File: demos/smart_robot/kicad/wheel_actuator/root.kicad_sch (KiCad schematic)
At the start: 9 parts, among them M1 WHEEL_MOTOR_DESIGN_ENVELOPE, U1 AT32M416, U2 DRV8323, U3 TCAN3413DR

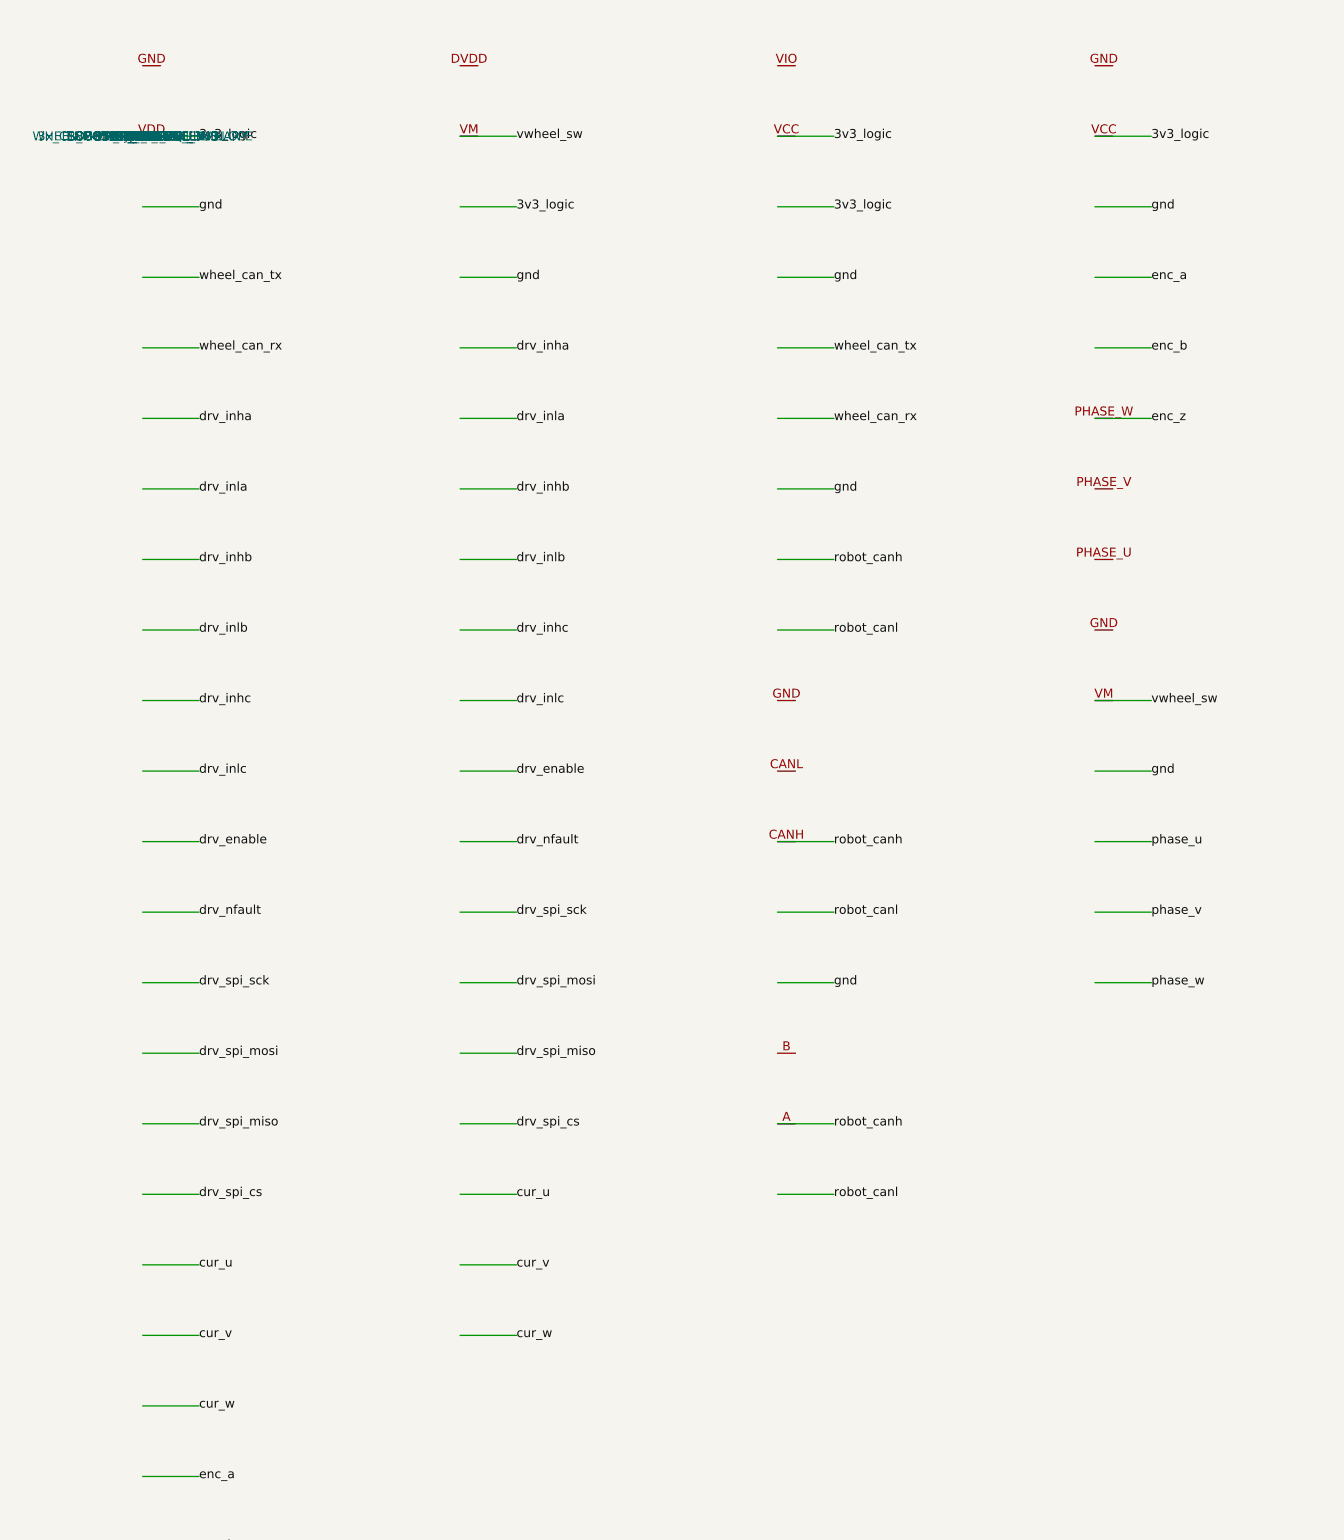
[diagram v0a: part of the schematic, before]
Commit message: Validate wheel current sense placement
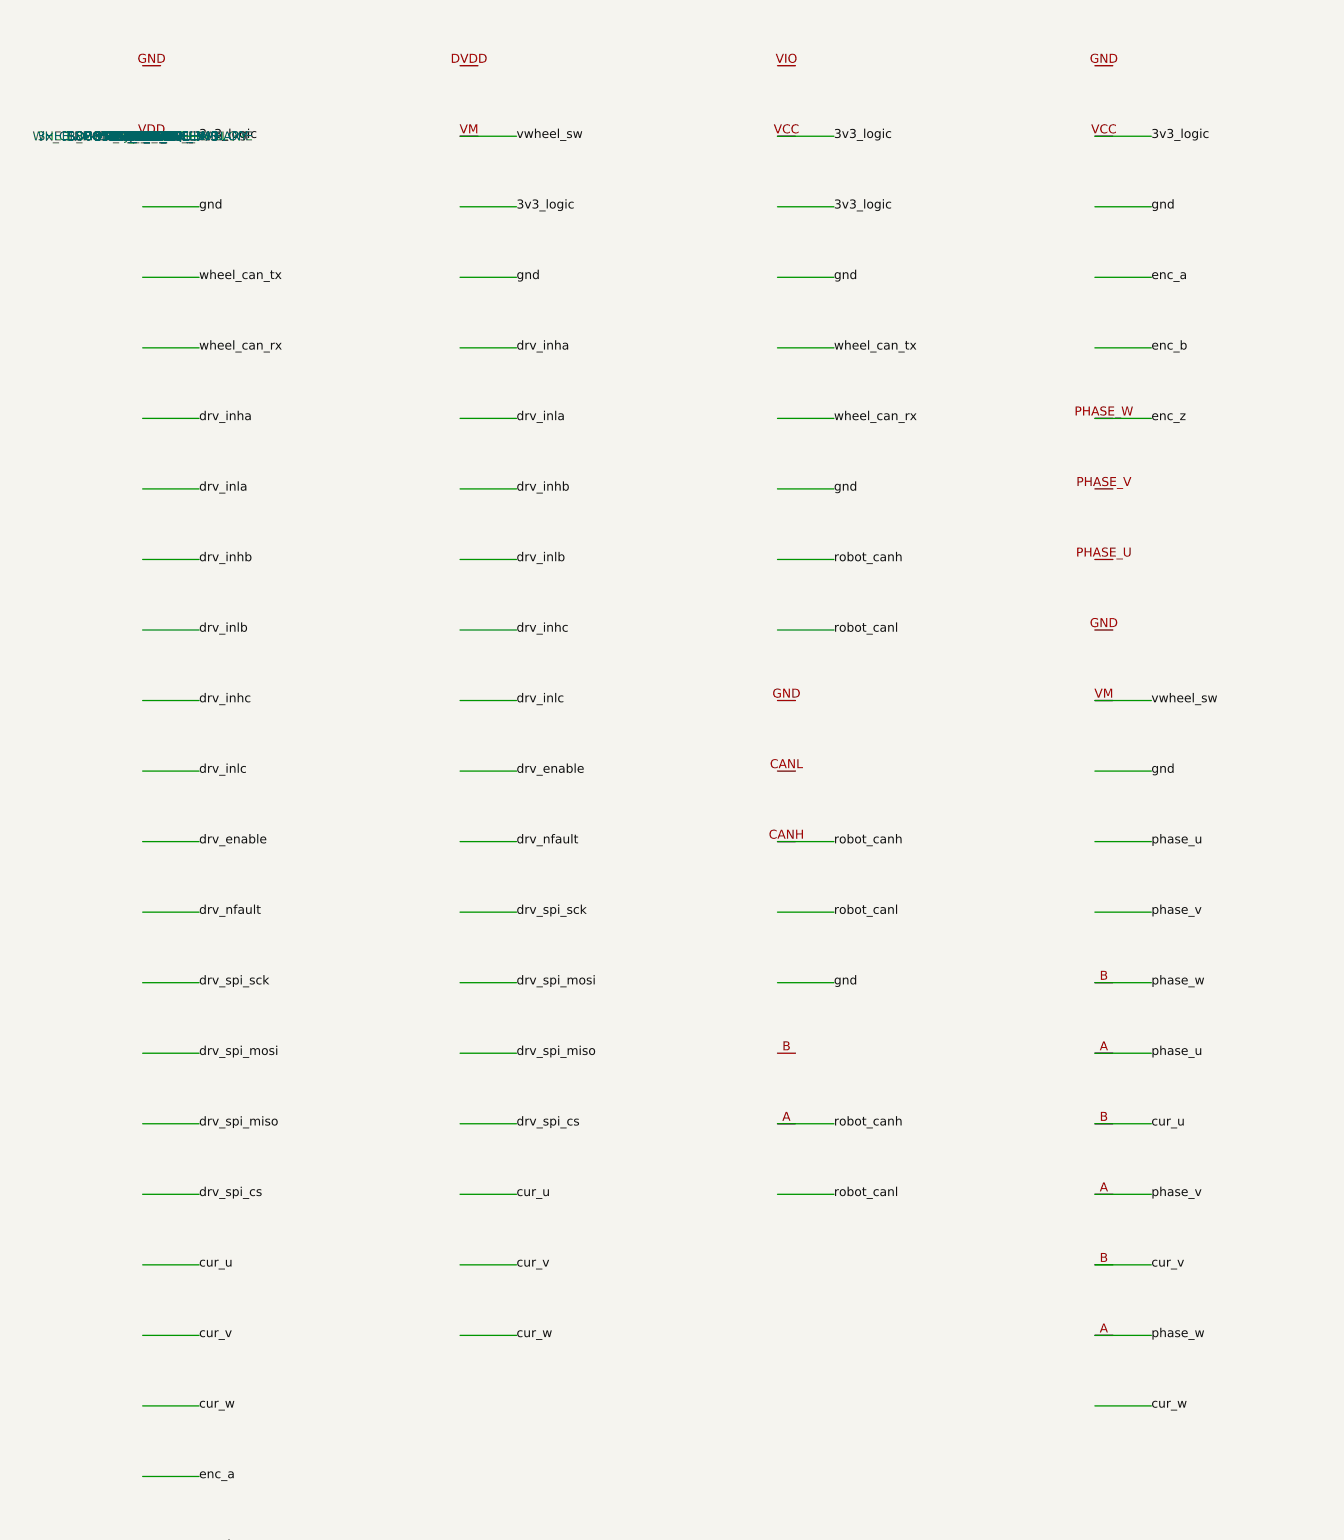
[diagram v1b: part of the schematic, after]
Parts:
- added RSHUNT_U, RSHUNT_V, RSHUNT_W: 5mR_1W, symbol CircuitCI:Resistor
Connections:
- net cur_u: now also RSHUNT_V.B
- net cur_v: now also RSHUNT_W.B
- net phase_u: now also RSHUNT_U.A
- net phase_v: now also RSHUNT_V.A
- net phase_w: now also RSHUNT_U.B, RSHUNT_W.A
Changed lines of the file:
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@@
     (property "Value" "3x_CSD88599Q5DC_PRELIMINARY")
     (pin "VM") (pin "GND") (pin "PHASE_U") (pin "PHASE_V") (pin "PHASE_W"))
+  (symbol (lib_id "CircuitCI:Resistor") (at 135 130 0)
+    (property "Reference" "RSHUNT_U")
+    (property "Value" "5mR_1W")
+    (pin "A") (pin "B"))
+  (symbol (lib_id "CircuitCI:Resistor") (at 135 150 0)
+    (property "Reference" "RSHUNT_V")
+    (property "Value" "5mR_1W")
+    (pin "A") (pin "B"))
+  (symbol (lib_id "CircuitCI:Resistor") (at 135 170 0)
+    (property "Reference" "RSHUNT_W")
+    (property "Value" "5mR_1W")
+    (pin "A") (pin "B"))
   (symbol (lib_id "CircuitCI:Wheel_Motor_Envelope") (at 180 80 0)
     (property "Reference" "M1")
@@
   (wire (pts (xy 135 110) (xy 143 110))) (label "phase_v" (at 143 110 0))
   (wire (pts (xy 135 120) (xy 143 120))) (label "phase_w" (at 143 120 0))
+  (wire (pts (xy 135 130) (xy 143 130))) (label "phase_u" (at 143 130 0))
+  (wire (pts (xy 135 140) (xy 143 140))) (label "cur_u" (at 143 140 0))
+  (wire (pts (xy 135 150) (xy 143 150))) (label "phase_v" (at 143 150 0))
+  (wire (pts (xy 135 160) (xy 143 160))) (label "cur_v" (at 143 160 0))
+  (wire (pts (xy 135 170) (xy 143 170))) (label "phase_w" (at 143 170 0))
+  (wire (pts (xy 135 180) (xy 143 180))) (label "cur_w" (at 143 180 0))
   (wire (pts (xy 180 0) (xy 188 0))) (label "vwheel_sw" (at 188 0 0))
   (wire (pts (xy 180 10) (xy 188 10))) (label "gnd" (at 188 10 0))

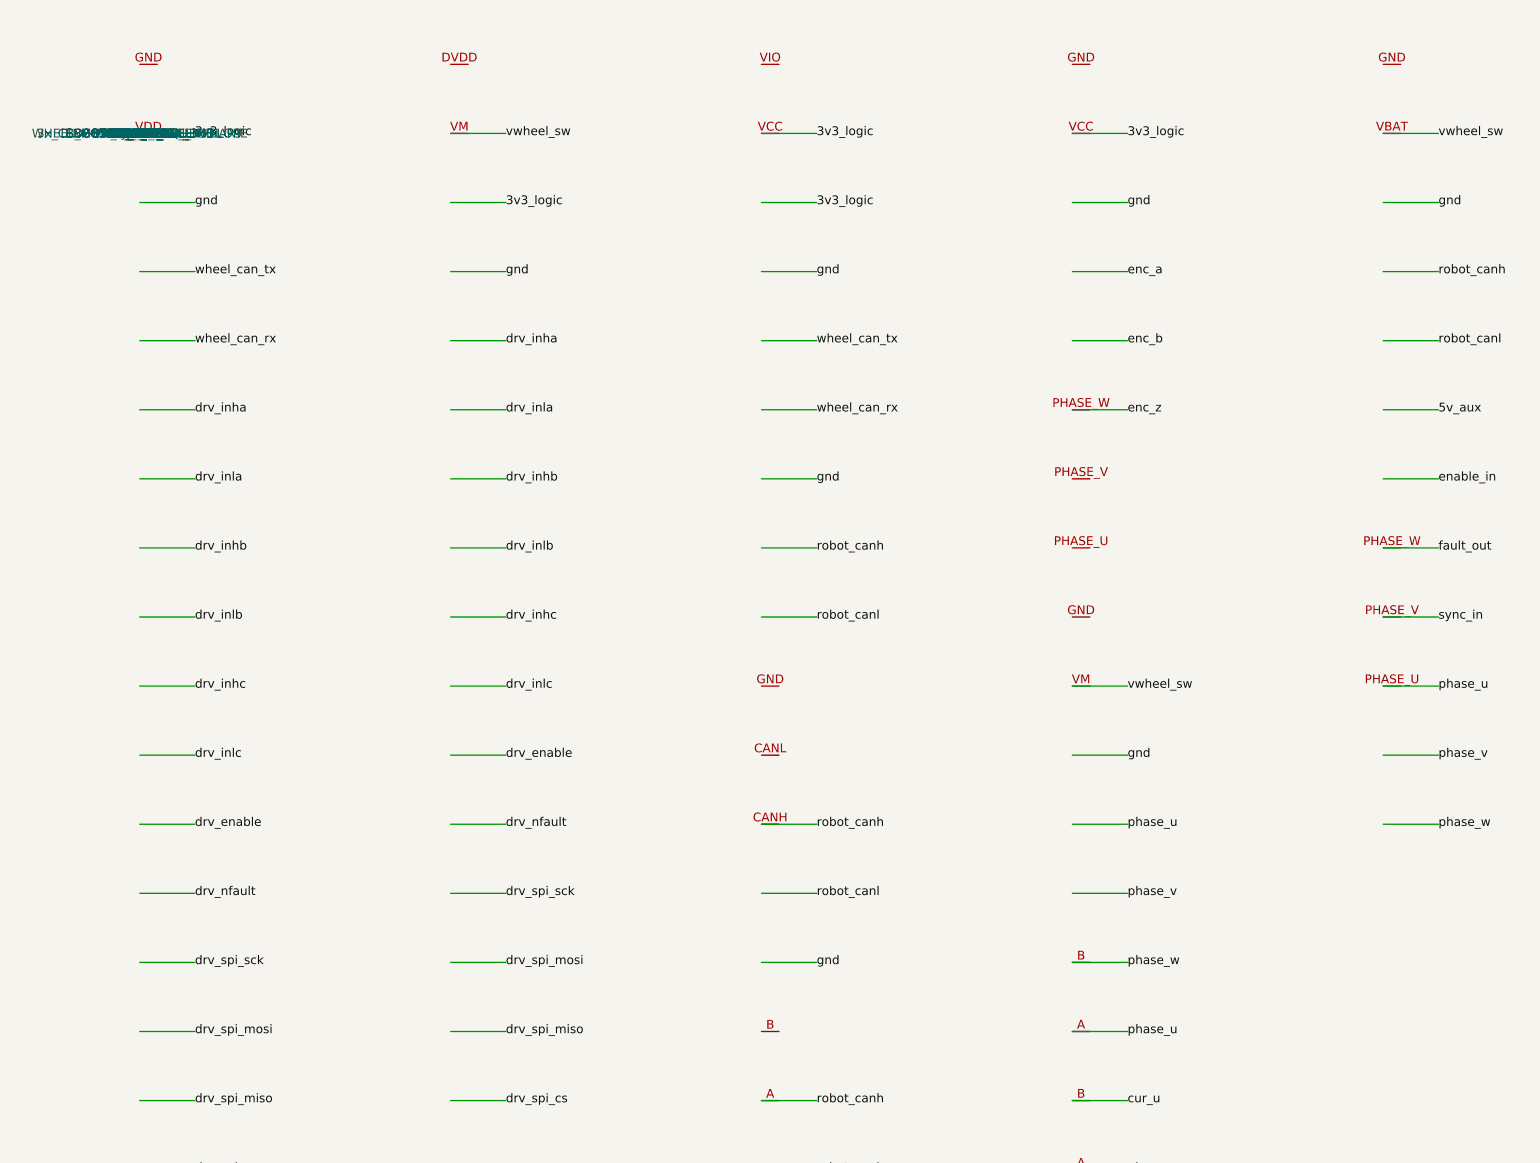
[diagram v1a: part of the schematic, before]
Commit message: Preserve wheel signoff gate through KiCad import
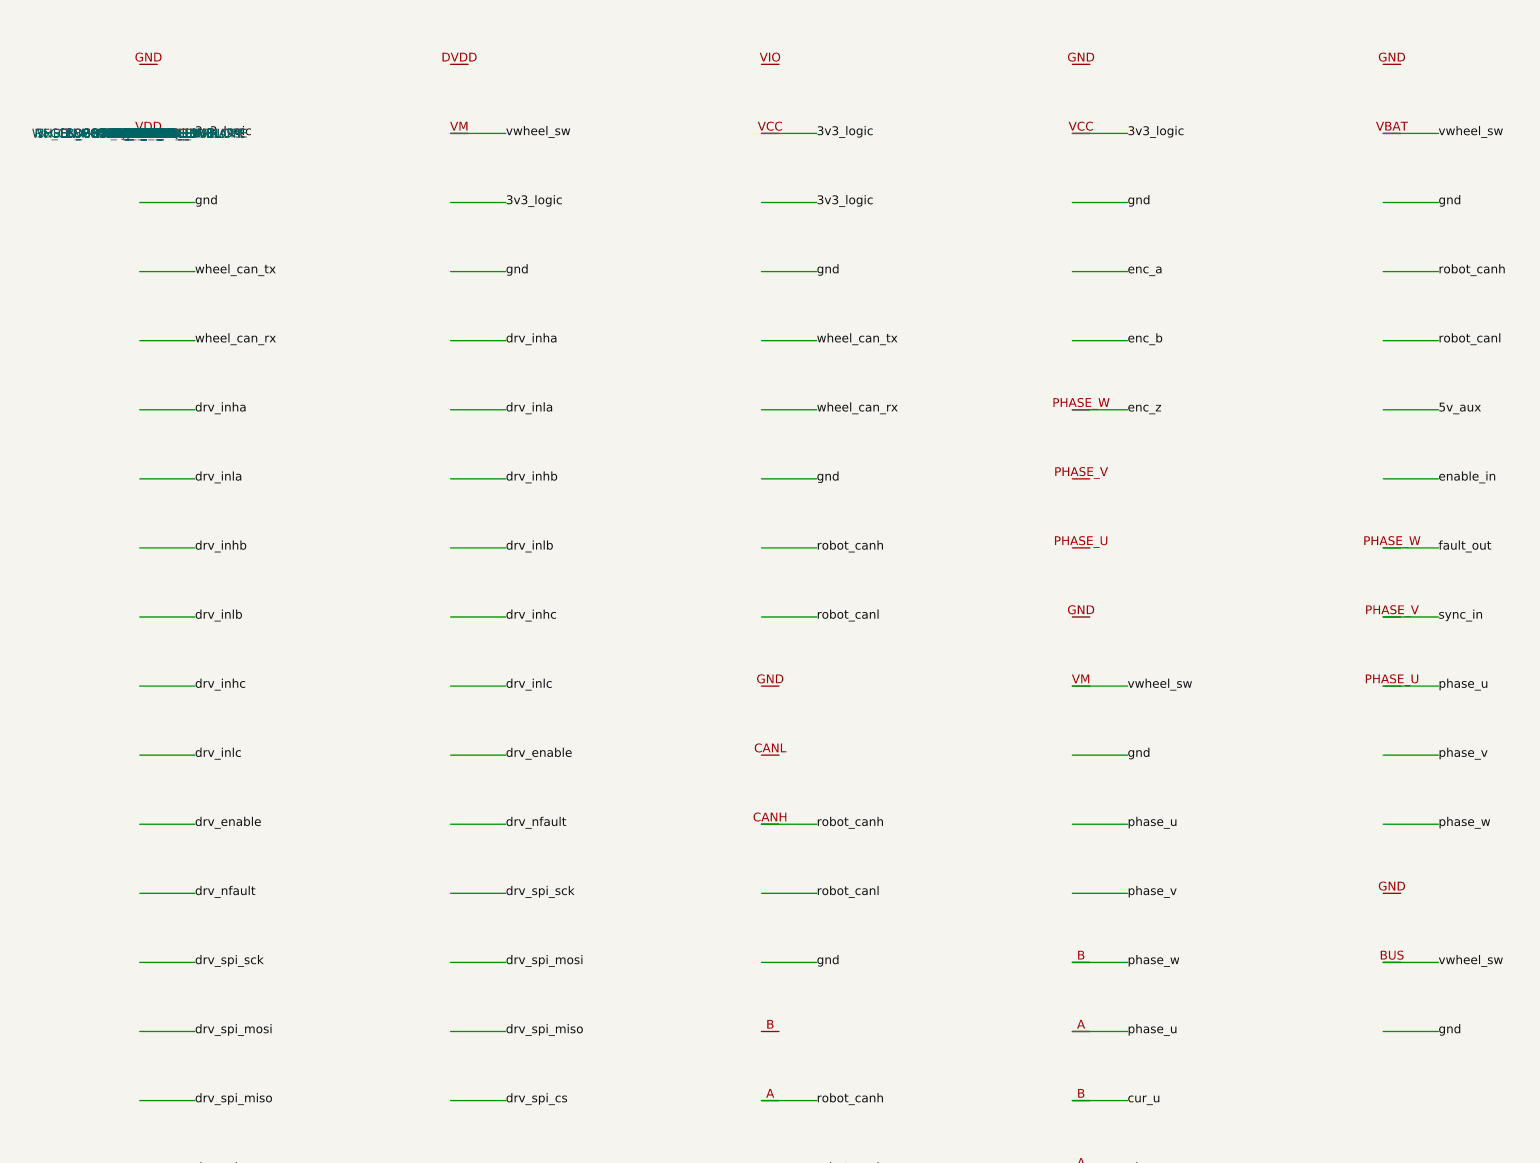
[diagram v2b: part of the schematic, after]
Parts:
- added REGEN1: REGEN_CLAMP_DESIGN_ENVELOPE, symbol CircuitCI:Regen_Clamp_Envelope
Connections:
- net vwheel_sw: now also REGEN1.BUS
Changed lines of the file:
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@@
     (property "Value" "3x_CSD88599Q5DC_PRELIMINARY")
     (pin "VM") (pin "GND") (pin "PHASE_U") (pin "PHASE_V") (pin "PHASE_W"))
+  (symbol (lib_id "CircuitCI:Regen_Clamp_Envelope") (at 180 120 0)
+    (property "Reference" "REGEN1")
+    (property "Value" "REGEN_CLAMP_DESIGN_ENVELOPE")
+    (pin "BUS") (pin "GND"))
   (symbol (lib_id "CircuitCI:Resistor") (at 135 130 0)
     (property "Reference" "RSHUNT_U")
@@
   (wire (pts (xy 180 90) (xy 188 90))) (label "phase_v" (at 188 90 0))
   (wire (pts (xy 180 100) (xy 188 100))) (label "phase_w" (at 188 100 0))
+  (wire (pts (xy 180 120) (xy 188 120))) (label "vwheel_sw" (at 188 120 0))
+  (wire (pts (xy 180 130) (xy 188 130))) (label "gnd" (at 188 130 0))
 )
